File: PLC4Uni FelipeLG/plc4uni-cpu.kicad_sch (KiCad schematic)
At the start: 1 part, among them U2 ESP32-S3-MINI-1U

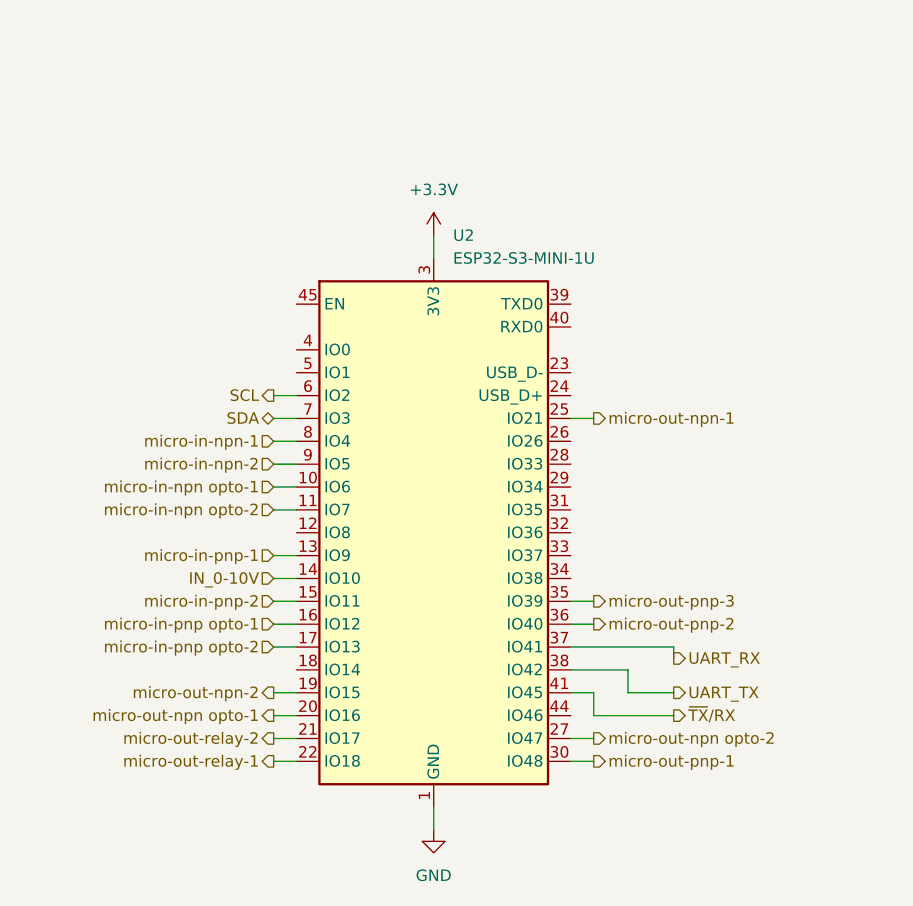
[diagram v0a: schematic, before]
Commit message: Add files via upload
Updated Circuitos corregidos y pistas agregadas
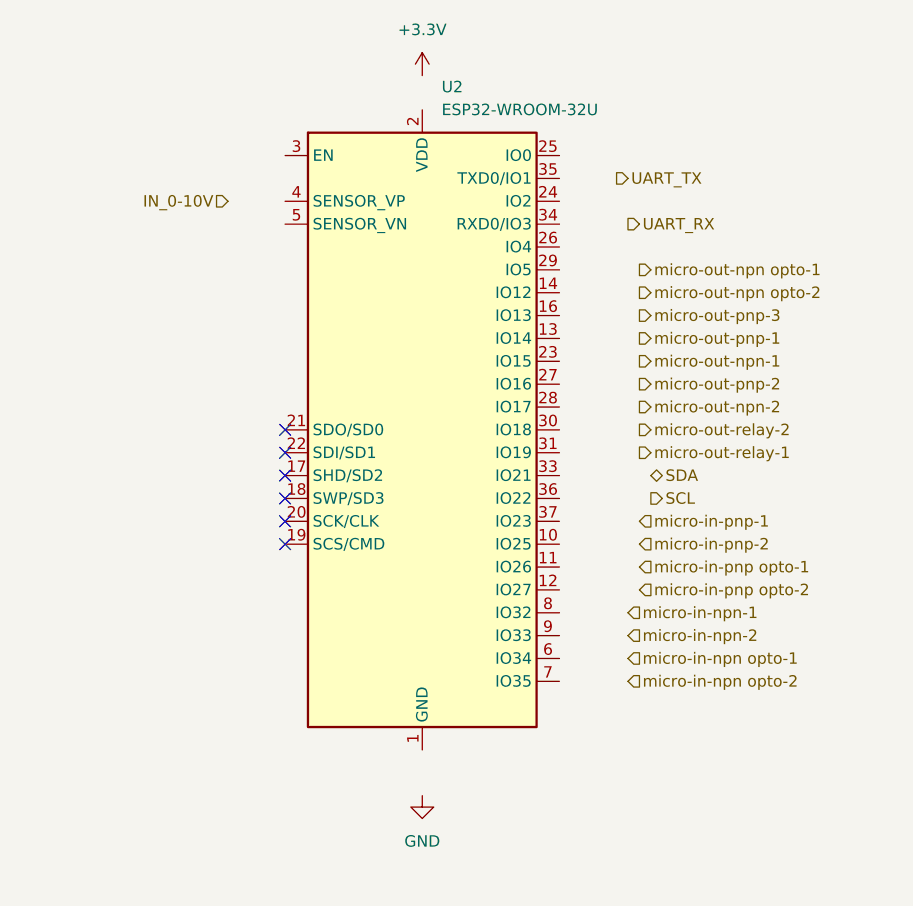
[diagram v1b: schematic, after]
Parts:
- removed U2: ESP32-S3-MINI-1U, RF_Module:ESP32-S2-MINI-1U, symbol RF_Module:ESP32-S3-MINI-1U
- added U2: ESP32-WROOM-32U, RF_Module:ESP32-WROOM-32U, symbol Espressif:ESP32-WROOM-32UU
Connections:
- new net: U2.1 (GND), U2.15 (GND), U2.38 (GND), U2.39 (GND)
- no-connect marks 0 -> 6
